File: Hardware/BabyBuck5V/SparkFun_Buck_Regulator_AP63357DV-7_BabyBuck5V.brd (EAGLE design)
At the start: 15.9 x 13.2 mm, 36 parts, among them U1 AP63357

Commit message: Added dimensions, ordering instructions, set board stackup.
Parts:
- added U$17: (no value), SparkFun-Aesthetics:ORDERING_INSTRUCTIONS
- moved FRAME1 19.4 mm to (20.7, -16.5)
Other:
- board text added: "Alex Brudner"
- board text added: "Board thickness is 0.8mm 4-Layer 1oz copper outer 1oz copper inner"
- board text added: "UNITS IN INCHES"
- board text added: "v01"
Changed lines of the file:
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@@
 <wire x1="11.049" y1="3.81" x2="12.573" y2="3.81" width="0.2032" layer="21"/>
 <rectangle x1="1.143" y1="0.254" x2="11.303" y2="12.954" layer="30"/>
+<text x="15.621" y="0.254" size="1.016" layer="16" font="vector" ratio="15" rot="MR0">v01</text>
+<dimension x1="0" y1="0" x2="13.843" y2="11.557" x3="-1.524" y3="5.7785" textsize="1.016" layer="47" dtype="vertical" unit="inch"/>
+<dimension x1="0" y1="0" x2="0" y2="13.208" x3="-4.064" y3="6.604" textsize="1.016" layer="47" dtype="vertical" unit="inch"/>
+<dimension x1="0" y1="0" x2="13.843" y2="11.557" x3="6.9215" y3="14.859" textsize="1.016" layer="47" dtype="horizontal" unit="inch"/>
+<dimension x1="0" y1="0" x2="15.875" y2="13.208" x3="7.9375" y3="17.907" textsize="1.016" layer="47" dtype="horizontal" unit="inch"/>
+<dimension x1="0" y1="0" x2="6.223" y2="6.604" x3="3.1115" y3="-1.905" textsize="1.016" layer="47" dtype="horizontal" unit="inch"/>
+<dimension x1="0" y1="0" x2="6.223" y2="6.604" x3="18.161" y3="3.302" textsize="1.016" layer="47" dtype="vertical" unit="inch"/>
+<dimension x1="1.143" y1="0.254" x2="11.303" y2="0.254" x3="6.223" y3="-5.969" textsize="1.016" layer="47" unit="inch"/>
+<dimension x1="1.143" y1="0.254" x2="1.143" y2="12.954" x3="22.098" y3="6.604" textsize="1.016" layer="47" unit="inch"/>
+<text x="2.286" y="23.495" size="1.016" layer="47" font="vector">UNITS IN INCHES</text>
+<text x="47.752" y="-16.637" size="1.778" layer="51" font="vector" ratio="15">Alex Brudner</text>
+<text x="26.924" y="22.225" size="1.778" layer="51" font="vector">Board thickness is 0.8mm
+4-Layer
+1oz copper outer
+1oz copper inner</text>
 </plain>
 <attributes>
@@
 </class>
 </classes>
-<designrules name="SparkFun-4-Layer-Minimum-JLCPCB">
+<designrules name="SparkFun-4-Layer-Minimum-JLCPCB *">
 <description language="en">&lt;b&gt;4 Layer Minimum Rules for JLCPCB&lt;/b&gt;
 &lt;p&gt;
@@
 &lt;/ul&gt;</description>
 <param name="layerSetup" value="(1*2*15*16)"/>
-<param name="mtCopper" value="0.035559375mm 0.035559375mm 0.035mm 0.035mm 0.035mm 0.035mm 0.035mm 0.035mm 0.035mm 0.035mm 0.035mm 0.035mm 0.035mm 0.035mm 0.035559375mm 0.035559375mm"/>
-<param name="mtIsolate" value="0.47751875mm 0.47751875mm 0.2mm 0.15mm 0.2mm 0.15mm 0.2mm 0.15mm 0.2mm 0.15mm 0.2mm 0.15mm 0.2mm 0.15mm 0.47751875mm"/>
+<param name="mtCopper" value="0.035mm 0.035mm 0.035mm 0.035mm 0.035mm 0.035mm 0.035mm 0.035mm 0.035mm 0.035mm 0.035mm 0.035mm 0.035mm 0.035mm 0.035mm 0.035mm"/>
+<param name="mtIsolate" value="0.2104mm 0.24mm 0.2mm 0.15mm 0.2mm 0.15mm 0.2mm 0.15mm 0.2mm 0.15mm 0.2mm 0.15mm 0.2mm 0.15mm 0.2104mm"/>
 <param name="mdWireWire" value="5mil"/>
 <param name="mdWirePad" value="5mil"/>
@@
 <element name="FD2" library="SparkFun-Aesthetics" package="FIDUCIAL-MICRO" value="FIDUCIALUFIDUCIAL" x="0.624840625" y="0.62738125" smashed="yes"/>
 <element name="FD4" library="SparkFun-Aesthetics" package="FIDUCIAL-MICRO" value="FIDUCIALUFIDUCIAL" x="0.624840625" y="0.62738125" smashed="yes" rot="MR0"/>
-<element name="FRAME1" library="SparkFun-Aesthetics" package="CREATIVE_COMMONS" value="FRAME-LEDGER" x="2.667" y="-9.271" smashed="yes">
-<attribute name="DESIGNER" value="Alex Brudner" x="82.677" y="-10.541" size="1.778" layer="27" display="off"/>
-<attribute name="REV" value="v01" x="82.677" y="-10.541" size="1.778" layer="27" display="off"/>
+<element name="FRAME1" library="SparkFun-Aesthetics" package="CREATIVE_COMMONS" value="FRAME-LEDGER" x="20.701" y="-16.51" smashed="yes">
+<attribute name="DESIGNER" value="Alex Brudner" x="100.711" y="-17.78" size="1.778" layer="27" display="off"/>
+<attribute name="REV" value="v01" x="100.711" y="-17.78" size="1.778" layer="27" display="off"/>
 </element>
 <element name="J1" library="SparkFun-Connectors" package="1X04_NO_SILK" value="" x="13.843" y="11.557" smashed="yes" rot="R270">
@@
 <element name="U$14" library="output" package="SPARKFUN0" value="" x="11.938" y="10.033" smashed="yes" rot="MR270"/>
 <element name="U$16" library="output" package="5V0" value="" x="11.938" y="0.889" smashed="yes" rot="MR270"/>
+<element name="U$17" library="SparkFun-Aesthetics" package="ORDERING_INSTRUCTIONS" value="" x="25.4" y="42.545" smashed="yes"/>
 </elements>
 <signals>
@@
 <via x="9.652" y="1.016" extent="1-16" drill="0.381"/>
 <via x="10.541" y="1.016" extent="1-16" drill="0.381"/>
-<via x="13.081" y="1.016" extent="1-16" drill="0.381"/>
-<via x="13.97" y="1.905" extent="1-16" drill="0.381"/>
-<via x="14.859" y="1.905" extent="1-16" drill="0.381"/>
-<via x="13.97" y="1.016" extent="1-16" drill="0.381"/>
-<via x="14.859" y="1.016" extent="1-16" drill="0.381"/>
+<via x="12.954" y="1.016" extent="1-16" drill="0.381"/>
+<via x="14.351" y="1.7272" extent="1-16" drill="0.381"/>
+<via x="15.24" y="1.7272" extent="1-16" drill="0.381"/>
 <polygon width="0.2032" layer="1" thermals="no" rank="2">
 <vertex x="8.763" y="0.381"/>
@@
 <vertex x="-0.127" y="-0.127"/>
 </polygon>
+<via x="13.462" y="1.7272" extent="1-16" drill="0.381"/>
 </signal>
 <signal name="EN">
@@
 </board>
 </drawing>
+<compatibility>
+<note version="6.3" minversion="6.2.2" severity="warning">
+Since Version 6.2.2 text objects can contain more than one line,
+which will not be processed correctly with this version.
+</note>
+</compatibility>
 </eagle>

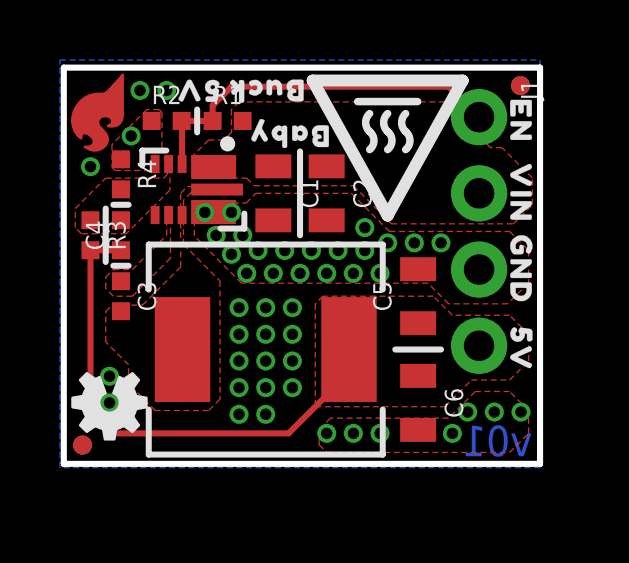
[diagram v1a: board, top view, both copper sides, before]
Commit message: Renumbered parts to match other schematic.
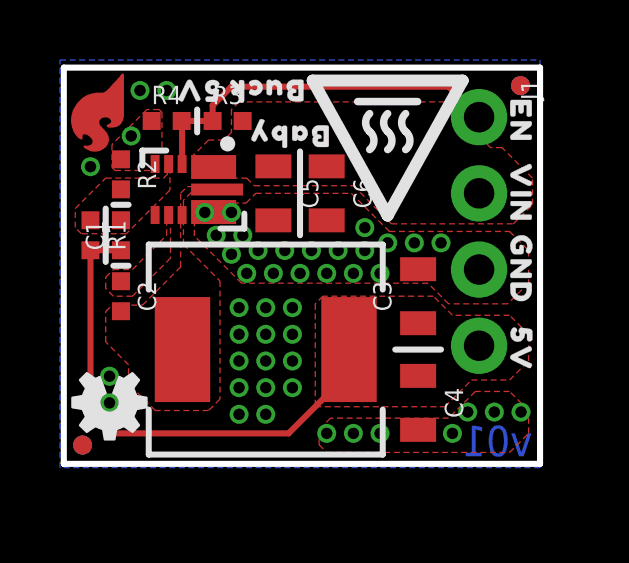
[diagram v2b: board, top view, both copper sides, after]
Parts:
- C1: value 4.7uF -> 47pF; device SparkFun-Capacitors:0805 -> SparkFun-Capacitors:0402-TIGHT
- C2: value 4.7uF -> 0.1uF; device SparkFun-Capacitors:0805 -> SparkFun-Capacitors:0402-TIGHT
- C3: value 0.1uF -> 22uF; device SparkFun-Capacitors:0402-TIGHT -> SparkFun-Capacitors:0805
- C4: value 47pF -> 22uF; device SparkFun-Capacitors:0402-TIGHT -> SparkFun-Capacitors:0805
- C5, C6: value 22uF -> 4.7uF
- R1: value 93.1k -> 150k; device Buck5V:0402-TIGHT -> SparkFun-Resistors:0402-TIGHT
- R2: value 22k -> 28.7k; device SparkFun-Resistors:0402-TIGHT -> Buck5V:0402-TIGHT
- R3: value 150k -> 93.1k; device SparkFun-Resistors:0402-TIGHT -> Buck5V:0402-TIGHT
- R4: value 28.7k -> 22k; device Buck5V:0402-TIGHT -> SparkFun-Resistors:0402-TIGHT
- moved C4 11.4 mm to (11.8, 2.03), turned to 270 degrees
- moved C3 9.91 mm to (11.8, 5.59), turned to 90 degrees
- moved C2 7.67 mm to (1.91, 5.59)
- moved C6 7.62 mm to (8.76, 9.02)
- moved R1 5.95 mm to (0.89, 7.62), turned to 270 degrees
- moved R3 5.95 mm to (5.46, 11.4), turned to 0 degrees
- moved C5 5.92 mm to (6.99, 9.02), turned to 270 degrees
- moved C1 5.27 mm to (1.91, 7.62), turned to 90 degrees
- moved R2 2.34 mm to (1.91, 9.65), turned to 270 degrees
- moved R4 2.34 mm to (3.43, 11.4), turned to 0 degrees
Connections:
- net 5V: now also C1.1, C3.1, R1.2; no longer C5.1, C6.1, R3.2
- net EN: now also R3.1, R4.2; no longer R1.1, R2.2
- net FB: now also C1.2, R1.1, R2.2; no longer C4.2, R3.1, R4.2
- net GND: now also C3.2, C4.2; no longer C1.2, C2.2
- net N$4: now also C2.1; no longer C3.1
- net SW: now also C2.2; no longer C3.2
- net VIN: now also C5.1, C6.1, R3.2; no longer C1.1, C2.1, R1.2
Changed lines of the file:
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@@
 </autorouter>
 <elements>
-<element name="C4" library="SparkFun-Capacitors" package="0402-TIGHT" value="47pF" x="1.905" y="7.62" smashed="yes" rot="R90">
+<element name="C1" library="SparkFun-Capacitors" package="0402-TIGHT" value="47pF" x="1.905" y="7.62" smashed="yes" rot="R90">
 <attribute name="NAME" x="1.343" y="7.62" size="0.6096" layer="25" font="vector" ratio="20" rot="R90" align="bottom-center"/>
 <attribute name="PROD_ID" value="CAP-15063" x="24.765" y="21.59" size="1.778" layer="27" rot="R90" display="off"/>
 <attribute name="VALUE" x="2.467" y="7.62" size="0.6096" layer="27" font="vector" ratio="20" rot="R90" align="top-center"/>
 </element>
-<element name="C3" library="SparkFun-Capacitors" package="0402-TIGHT" value="0.1uF" x="1.905" y="5.588" smashed="yes" rot="R270">
+<element name="C2" library="SparkFun-Capacitors" package="0402-TIGHT" value="0.1uF" x="1.905" y="5.588" smashed="yes" rot="R270">
 <attribute name="NAME" x="2.467" y="5.588" size="0.6096" layer="25" font="vector" ratio="20" rot="R270" align="bottom-center"/>
 <attribute name="PROD_ID" value="CAP-12416" x="-15.875" y="-36.322" size="1.778" layer="27" rot="R270" display="off"/>
 <attribute name="VALUE" x="1.343" y="5.588" size="0.6096" layer="27" font="vector" ratio="20" rot="R270" align="top-center"/>
 </element>
-<element name="C5" library="SparkFun-Capacitors" package="0805" value="22uF" x="11.811" y="5.588" smashed="yes" rot="R90">
+<element name="C3" library="SparkFun-Capacitors" package="0805" value="22uF" x="11.811" y="5.588" smashed="yes" rot="R90">
 <attribute name="NAME" x="10.922" y="5.588" size="0.6096" layer="25" font="vector" ratio="20" rot="R90" align="bottom-center"/>
 <attribute name="PROD_ID" value="CAP-14260" x="23.241" y="41.148" size="1.778" layer="27" rot="R90" display="off"/>
 <attribute name="VALUE" x="12.7" y="5.588" size="0.6096" layer="27" font="vector" ratio="20" rot="R90" align="top-center"/>
 </element>
-<element name="C6" library="SparkFun-Capacitors" package="0805" value="22uF" x="11.811" y="2.032" smashed="yes" rot="R270">
+<element name="C4" library="SparkFun-Capacitors" package="0805" value="22uF" x="11.811" y="2.032" smashed="yes" rot="R270">
 <attribute name="NAME" x="12.7" y="2.032" size="0.6096" layer="25" font="vector" ratio="20" rot="R270" align="bottom-center"/>
 <attribute name="PROD_ID" value="CAP-14260" x="0.381" y="-37.338" size="1.778" layer="27" rot="R270" display="off"/>
 <attribute name="VALUE" x="10.922" y="2.032" size="0.6096" layer="27" font="vector" ratio="20" rot="R270" align="top-center"/>
 </element>
-<element name="C2" library="SparkFun-Capacitors" package="0805" value="4.7uF" x="8.763" y="9.017" smashed="yes" rot="R270">
+<element name="C6" library="SparkFun-Capacitors" package="0805" value="4.7uF" x="8.763" y="9.017" smashed="yes" rot="R270">
 <attribute name="NAME" x="9.652" y="9.017" size="0.6096" layer="25" font="vector" ratio="20" rot="R270" align="bottom-center"/>
 <attribute name="PROD_ID" value="CAP-15457" x="-2.667" y="-34.163" size="1.778" layer="27" rot="R270" display="off"/>
 <attribute name="VALUE" x="7.874" y="9.017" size="0.6096" layer="27" font="vector" ratio="20" rot="R270" align="top-center"/>
 </element>
-<element name="C1" library="SparkFun-Capacitors" package="0805" value="4.7uF" x="6.985" y="9.017" smashed="yes" rot="R270">
+<element name="C5" library="SparkFun-Capacitors" package="0805" value="4.7uF" x="6.985" y="9.017" smashed="yes" rot="R270">
 <attribute name="NAME" x="7.874" y="9.017" size="0.6096" layer="25" font="vector" ratio="20" rot="R270" align="bottom-center"/>
 <attribute name="PROD_ID" value="CAP-15457" x="-12.065" y="-6.223" size="1.778" layer="27" rot="R270" display="off"/>
@@
 <element name="LOGO2" library="SparkFun-Aesthetics" package="OSHW-LOGO-MINI" value="OSHW-LOGOMINI" x="1.524" y="2.032" smashed="yes" rot="R180"/>
 <element name="LOGO1" library="SparkFun-Aesthetics" package="BLANK" value="SFE_LOGO_NAME_FLAMEBLANK" x="14.859" y="0.254" smashed="yes"/>
-<element name="R3" library="SparkFun-Resistors" package="0402-TIGHT" value="150k" x="0.889" y="7.62" smashed="yes" rot="R270">
+<element name="R1" library="SparkFun-Resistors" package="0402-TIGHT" value="150k" x="0.889" y="7.62" smashed="yes" rot="R270">
 <attribute name="NAME" x="1.451" y="7.62" size="0.6096" layer="25" font="vector" ratio="20" rot="R270" align="bottom-center"/>
 <attribute name="PROD_ID" value="RES-15093" x="-16.891" y="-36.83" size="1.778" layer="27" rot="R270" display="off"/>
@@
 <attribute name="VALUE" x="0.327" y="7.62" size="0.6096" layer="27" font="vector" ratio="20" rot="R270" align="top-center"/>
 </element>
-<element name="R4" library="Buck5V" package="0402-TIGHT" value="28.7k" x="1.905" y="9.652" smashed="yes" rot="R270">
+<element name="R2" library="Buck5V" package="0402-TIGHT" value="28.7k" x="1.905" y="9.652" smashed="yes" rot="R270">
 <attribute name="NAME" x="2.467" y="9.652" size="0.6096" layer="25" font="vector" ratio="20" rot="R270" align="bottom-center"/>
 <attribute name="PROD_ID" value="RES-" x="-15.875" y="-24.638" size="1.778" layer="27" rot="R270" display="off"/>
 <attribute name="VALUE" x="1.343" y="9.652" size="0.6096" layer="27" font="vector" ratio="20" rot="R270" align="top-center"/>
 </element>
-<element name="R1" library="Buck5V" package="0402-TIGHT" value="93.1k" x="5.461" y="11.43" smashed="yes">
+<element name="R3" library="Buck5V" package="0402-TIGHT" value="93.1k" x="5.461" y="11.43" smashed="yes">
 <attribute name="NAME" x="5.461" y="11.992" size="0.6096" layer="25" font="vector" ratio="20" align="bottom-center"/>
 <attribute name="PROD_ID" value="RES-" x="43.561" y="-6.35" size="1.778" layer="27" display="off"/>
 <attribute name="VALUE" x="5.461" y="10.868" size="0.6096" layer="27" font="vector" ratio="20" align="top-center"/>
 </element>
-<element name="R2" library="SparkFun-Resistors" package="0402-TIGHT" value="22k" x="3.429" y="11.43" smashed="yes">
+<element name="R4" library="SparkFun-Resistors" package="0402-TIGHT" value="22k" x="3.429" y="11.43" smashed="yes">
 <attribute name="NAME" x="3.429" y="11.992" size="0.6096" layer="25" font="vector" ratio="20" align="bottom-center"/>
 <attribute name="PROD_ID" value="RES-14281" x="19.939" y="-11.43" size="1.778" layer="27" display="off"/>
@@
 <signal name="FB">
 <contactref element="U1" pad="P$3"/>
-<contactref element="R3" pad="1"/>
-<contactref element="R4" pad="2"/>
-<contactref element="C4" pad="2"/>
+<contactref element="R1" pad="1"/>
+<contactref element="R2" pad="2"/>
+<contactref element="C1" pad="2"/>
 <polygon width="0.2032" layer="1" thermals="no" rank="2">
 <vertex x="3.53821875" y="10.19301875"/>
@@
 <contactref element="U1" pad="P$7"/>
 <contactref element="U1" pad="P$9"/>
-<contactref element="C3" pad="2"/>
+<contactref element="C2" pad="2"/>
 <polygon width="0.2032" layer="1" thermals="no">
 <vertex x="5.87501875" y="9.24051875"/>
@@
 </signal>
 <signal name="N$4">
-<contactref element="C3" pad="1"/>
+<contactref element="C2" pad="1"/>
 <contactref element="U1" pad="P$6"/>
 <polygon width="0.2032" layer="1" thermals="no" rank="2">
@@
 </signal>
 <signal name="GND">
-<contactref element="R2" pad="1"/>
+<contactref element="R4" pad="1"/>
 <contactref element="U1" pad="P$8"/>
 <contactref element="U1" pad="P$4"/>
-<contactref element="R4" pad="1"/>
+<contactref element="R2" pad="1"/>
+<contactref element="C4" pad="2"/>
+<contactref element="C3" pad="2"/>
 <contactref element="C6" pad="2"/>
+<contactref element="J1" pad="3"/>
 <contactref element="C5" pad="2"/>
-<contactref element="C2" pad="2"/>
-<contactref element="J1" pad="3"/>
-<contactref element="C1" pad="2"/>
 <polygon width="0.2032" layer="1" thermals="no" rank="3">
 <vertex x="4.351021875" y="8.691878125"/>
@@
 <signal name="EN">
 <contactref element="U1" pad="P$2"/>
-<contactref element="R1" pad="1"/>
-<contactref element="R2" pad="2"/>
+<contactref element="R3" pad="1"/>
+<contactref element="R4" pad="2"/>
 <contactref element="J1" pad="1"/>
 <wire x1="3.929" y1="11.43" x2="3.943" y2="11.416" width="0.2032" layer="1"/>
@@
 </signal>
 <signal name="VIN">
-<contactref element="R1" pad="2"/>
+<contactref element="R3" pad="2"/>
 <contactref element="U1" pad="P$1"/>
-<contactref element="C2" pad="1"/>
-<contactref element="C1" pad="1"/>
+<contactref element="C6" pad="1"/>
+<contactref element="C5" pad="1"/>
 <contactref element="J1" pad="2"/>
 <polygon width="0.2032" layer="1" thermals="no" rank="2">
@@
 </signal>
 <signal name="5V">
-<contactref element="R3" pad="2"/>
+<contactref element="R1" pad="2"/>
+<contactref element="C1" pad="1"/>
+<contactref element="L1" pad="P$2"/>
 <contactref element="C4" pad="1"/>
-<contactref element="L1" pad="P$2"/>
-<contactref element="C6" pad="1"/>
-<contactref element="C5" pad="1"/>
+<contactref element="C3" pad="1"/>
 <contactref element="J1" pad="4"/>
 <polygon width="0.254" layer="1" isolate="0.2032" thermals="no">

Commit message: v01 changes implemented.
Schematic:
Add note for LED jumper
Add green wire for EN
Section titles center anchor
Rename Regulator section
Layout:
Increase selective solder width
Move 1x1 thermal pad
Make silk labels more explicit
Add "CAUTION: HOT" or just "HOT" silk
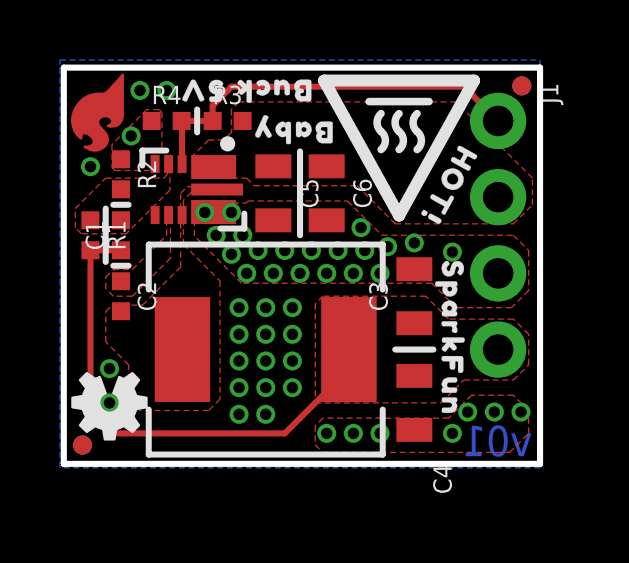
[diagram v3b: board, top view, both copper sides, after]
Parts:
- removed U$11, U$16: (no value), output:5V0
- removed U$12: (no value), output:VIN0
- removed U$13: (no value), output:GND0
- removed U$15: (no value), output:BABYBUCK0
- U$10: device output:EN0 -> output:HOT##7
- U$2: device output:EN0 -> output:#EN_#10
- U$3: device output:VIN0 -> output:#VIN_#11
- U$4: device output:GND0 -> output:#GND#13
- U$5: device output:5V0 -> output:#_5V_#6
- moved U$14 5.93 mm to (13.0, 4.19), flipped to the top
- moved U$10 3.24 mm to (12.8, 9.27), flipped to the top, turned to 241 degrees
- moved U$3 2.67 mm to (12.6, 8.89), flipped to the bottom, turned to 180 degrees
- moved U$5 2.67 mm to (12.6, 3.81), flipped to the bottom, turned to 180 degrees
- moved U$2 2.54 mm to (12.7, 11.4), flipped to the bottom, turned to 180 degrees
- moved U$4 2.29 mm to (13.0, 6.35), flipped to the bottom, turned to 90 degrees
- moved J1 0.65 mm to (14.5, 11.4)
- moved U$8 0.38 mm to (11.2, 11.2)
- moved U$7 0.25 mm to (6.99, 12.4)
- moved U$6 0.18 mm to (7.62, 11.0)
- moved C3 0.13 mm to (11.7, 5.59)
- moved C4 0.13 mm to (11.7, 2.03)
- moved U$9 0.13 mm to (4.57, 12.4)
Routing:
- net EN: track 12.6 -> 13.2 mm
